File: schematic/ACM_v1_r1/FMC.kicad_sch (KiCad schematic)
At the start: 2 parts, among them J5 DF40C-60DS-0.4V(51), J6 DF40C-60DS-0.4V(51)

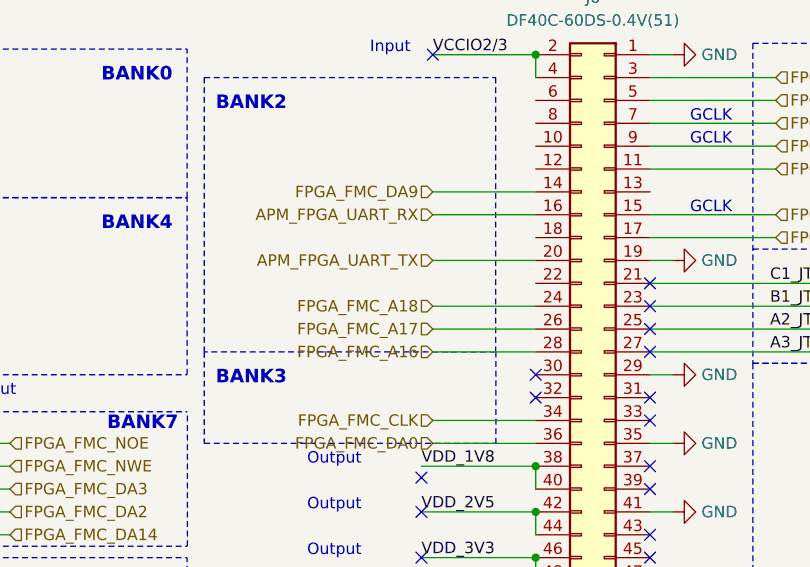
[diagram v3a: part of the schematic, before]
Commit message: adding renders and render script
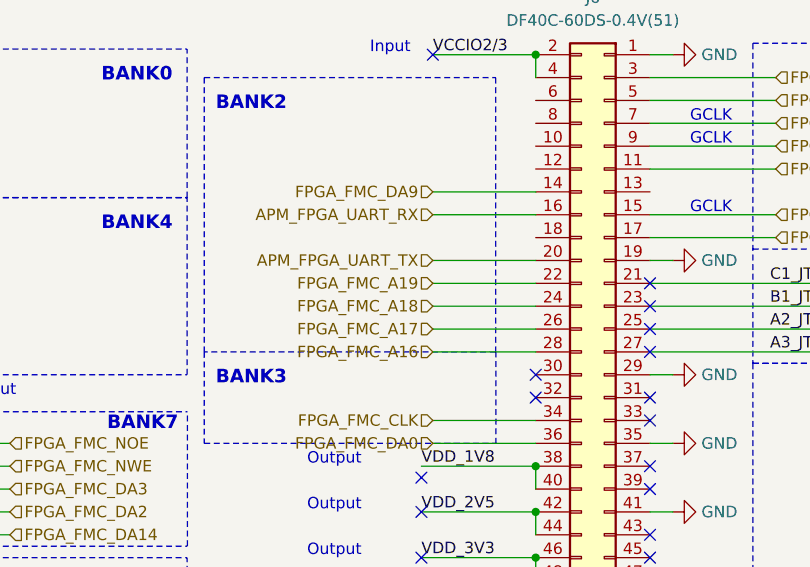
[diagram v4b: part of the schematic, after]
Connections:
- net FPGA_FMC_A19: now reaches J6.22 (Pin_22)
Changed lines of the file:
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@@
+	(wire
+		(pts
+			(xy 171.45 77.47) (xy 182.88 77.47)
+		)
+		(stroke
+			(width 0)
+			(type default)
+		)
+	)
 	(wire
 		(pts
@@
 		(effects
 			(font
+				(size 1.27 1.27)
+			)
+			(justify right)
+		)
+	)
+	(hierarchical_label "FPGA_FMC_A19"
+		(shape input)
+		(at 171.45 77.47 180)
+		(effects
+			(font
